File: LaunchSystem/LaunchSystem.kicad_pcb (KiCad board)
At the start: 2 copper layers, 125 x 50.5 mm, 24 parts, among them J1 GND - Ignition, J10 GND - Ignition, J2 VCC - +9V - Ignition, J5 VCC - 9V IN - ESP, J6 VCC - 9V IN - Ignition, J7 VCC - 9V IN - Ignition, J8 GND - Ignition, J9 GND - ESP, K1 43.41.7.005.2000, Q1 BC547, SW1 SW_SPDT, U2 L7805

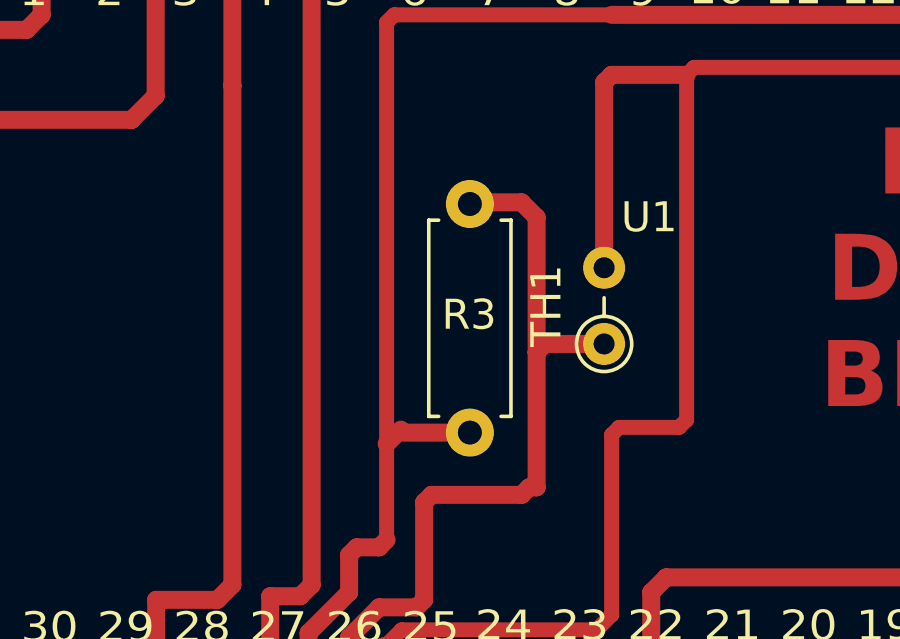
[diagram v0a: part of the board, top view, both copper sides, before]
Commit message: Update KiCad PWR section, footprints & nets
Add KiCad lock/history ignores to .gitignore. Major PCB changes: rename nets (GPIO35 -> 3.3v), add axial resistor footprint, replace/update TO-220 footprint for L7805 and update related pads/traces/zones. Schematic updates: bump sch revision to V3, add title block/date/rev/company, reposition components/junctions/wires, add PWR section label and a resistor symbol (R2), move PWR_FLAG and connectors. Overall: layout cleanup, footprint corrections and schematic revision to reflect PWR section rework.
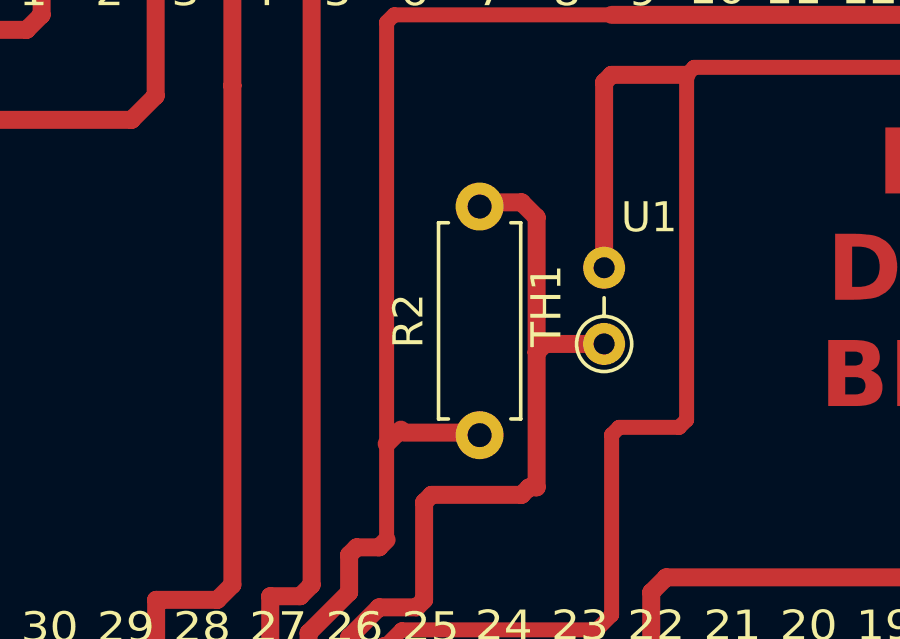
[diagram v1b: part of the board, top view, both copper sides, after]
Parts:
- removed R3: R 10k, Resistor_THT:R_Axial_DIN0207_L6.3mm_D2.5mm_P7.62mm_Horizontal
- added R2: R 10k, Resistor_THT:R_Axial_DIN0207_L6.3mm_D2.5mm_P7.62mm_Horizontal, F.Cu at (221.6, 98.0)
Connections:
- TH1 pad 1: Net-(U1-GPIO35) -> Net-(U1-3.3v)
- U1 pad 26: Net-(U1-GPIO35) -> Net-(U1-3.3v)
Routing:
- net Net-(U1-3.3v): track 294.4 -> 320.5 mm
- net Net-(U1-GPIO35): track 26.2 -> 0.00 mm

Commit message: Update LaunchSystem.kicad_pcb
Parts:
- J10, J8: value GND - Ignition -> GND - Ignition - Battery
- J6, J7: value VCC - 9V IN - Ignition -> VCC - 9V IN - Ignition Battery
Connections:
- R2 pad 2: Net-(U1-3.3v) -> Net-(U1-GPIO35)
- TH1 pad 1: Net-(U1-3.3v) -> Net-(U1-GPIO35)
- U1 pad 26: Net-(U1-3.3v) -> Net-(U1-GPIO35)
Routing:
- net Net-(U1-3.3v): track 320.5 -> 294.4 mm
- net Net-(U1-GPIO35): track 0.00 -> 26.2 mm
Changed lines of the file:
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@@
 			)
 		)
-		(property "Value" "VCC - 9V IN - Ignition"
+		(property "Value" "VCC - 9V IN - Ignition Battery"
 			(at 0 2.05 0)
 			(layer "F.Fab")
@@
 			(layers "*.Cu" "*.Mask")
 			(remove_unused_layers no)
-			(net "Net-(U1-3.3v)")
+			(net "Net-(U1-GPIO35)")
 			(pinfunction "GPIO35_26")
 			(pintype "bidirectional")
@@
 			(layers "*.Cu" "*.Mask")
 			(remove_unused_layers no)
-			(net "Net-(U1-3.3v)")
+			(net "Net-(U1-GPIO35)")
 			(pintype "passive")
 		)
@@
 			)
 		)
-		(property "Value" "VCC - 9V IN - Ignition"
+		(property "Value" "VCC - 9V IN - Ignition Battery"
 			(at 0 2.05 0)
 			(layer "F.Fab")
@@
 			(layers "*.Cu" "*.Mask")
 			(remove_unused_layers no)
-			(net "Net-(U1-3.3v)")
+			(net "Net-(U1-GPIO35)")
 			(pintype "passive")
 		)
@@
 			)
 		)
-		(property "Value" "GND - Ignition"
+		(property "Value" "GND - Ignition - Battery"
 			(at 0 2.05 0)
 			(layer "F.Fab")
@@
 			)
 		)
-		(property "Value" "GND - Ignition"
+		(property "Value" "GND - Ignition - Battery"
 			(at 6.975 6.975 0)
 			(layer "F.Fab")
@@
 	)
 	(segment
-		(start 223.78 94.97)
-		(end 223.5 95.25)
-		(width 0.6)
-		(layer "F.Cu")
-		(net "Net-(U1-3.3v)")
-	)
-	(segment
 		(start 210.818 108.318)
 		(end 210.818 103.5)
@@
 	)
 	(segment
-		(start 217.16 106.5)
-		(end 217.25 106.41)
-		(width 0.6)
-		(layer "F.Cu")
-		(net "Net-(U1-3.3v)")
-	)
-	(segment
-		(start 223.25 99.75)
-		(end 223.5 99.75)
-		(width 0.6)
-		(layer "F.Cu")
-		(net "Net-(U1-3.3v)")
-	)
-	(segment
-		(start 217.25 104.75)
-		(end 218.25 103.75)
-		(width 0.6)
-		(layer "F.Cu")
-		(net "Net-(U1-3.3v)")
-	)
-	(segment
 		(start 167.25 115.25)
 		(end 166.25 116.25)
@@
 	)
 	(segment
-		(start 221.33 90.25)
-		(end 223 90.25)
-		(width 0.6)
-		(layer "F.Cu")
-		(net "Net-(U1-3.3v)")
-	)
-	(segment
 		(start 217.25 103.25)
 		(end 217.25 102)
@@
 	)
 	(segment
-		(start 218.25 103.75)
-		(end 219.5 103.75)
-		(width 0.6)
-		(layer "F.Cu")
-		(net "Net-(U1-3.3v)")
-	)
-	(segment
 		(start 213.3586 86.3586)
 		(end 213.358 86.358)
@@
 	)
 	(segment
-		(start 217.25 106.41)
-		(end 217.25 104.75)
-		(width 0.6)
-		(layer "F.Cu")
-		(net "Net-(U1-3.3v)")
-	)
-	(segment
 		(start 141 117)
 		(end 140 118)
@@
 	)
 	(segment
-		(start 225.75 94.97)
-		(end 223.78 94.97)
-		(width 0.6)
-		(layer "F.Cu")
-		(net "Net-(U1-3.3v)")
-	)
-	(segment
-		(start 219.75 100.25)
-		(end 220 100)
-		(width 0.6)
-		(layer "F.Cu")
-		(net "Net-(U1-3.3v)")
-	)
-	(segment
 		(start 218.5 98.3)
 		(end 218.5 101.5)
@@
 	)
 	(segment
-		(start 219.75 103.5)
-		(end 219.75 100.25)
-		(width 0.6)
-		(layer "F.Cu")
-		(net "Net-(U1-3.3v)")
-	)
-	(segment
 		(start 218.5 84.25)
 		(end 218.75 84)
@@
 	)
 	(segment
-		(start 223.5 99.75)
-		(end 223.5 95.25)
-		(width 0.6)
-		(layer "F.Cu")
-		(net "Net-(U1-3.3v)")
-	)
-	(segment
 		(start 210.818 103.5)
 		(end 212.8586 103.5)
@@
 	)
 	(segment
-		(start 223 90.25)
-		(end 223.5 90.75)
-		(width 0.6)
-		(layer "F.Cu")
-		(net "Net-(U1-3.3v)")
-	)
-	(segment
-		(start 220 100)
-		(end 223 100)
-		(width 0.6)
-		(layer "F.Cu")
-		(net "Net-(U1-3.3v)")
-	)
-	(segment
 		(start 138.5 118.5)
 		(end 138.5 122.5)
@@
 	)
 	(segment
-		(start 223 100)
-		(end 223.25 99.75)
-		(width 0.6)
-		(layer "F.Cu")
-		(net "Net-(U1-3.3v)")
-	)
-	(segment
-		(start 219.5 103.75)
-		(end 219.75 103.5)
-		(width 0.6)
-		(layer "F.Cu")
-		(net "Net-(U1-3.3v)")
-	)
-	(segment
-		(start 223.5 90.75)
-		(end 223.5 95.25)
-		(width 0.6)
-		(layer "F.Cu")
-		(net "Net-(U1-3.3v)")
-	)
-	(segment
 		(start 131 77.5)
 		(end 130 78.5)
@@
 	)
 	(segment
-		(start 221.275 90.305)
-		(end 221.5 90.08)
-		(width 0.6)
-		(layer "F.Cu")
-		(net "Net-(U1-3.3v)")
-	)
-	(segment
-		(start 221.275 90.305)
-		(end 221.33 90.25)
-		(width 0.6)
-		(layer "F.Cu")
-		(net "Net-(U1-3.3v)")
-	)
-	(segment
 		(start 213.3586 103)
 		(end 213.3586 86.3586)
@@
 	)
 	(segment
+		(start 223.78 94.97)
+		(end 223.5 95.25)
+		(width 0.6)
+		(layer "F.Cu")
+		(net "Net-(U1-GPIO35)")
+	)
+	(segment
+		(start 217.16 106.5)
+		(end 217.25 106.41)
+		(width 0.6)
+		(layer "F.Cu")
+		(net "Net-(U1-GPIO35)")
+	)
+	(segment
+		(start 223.25 99.75)
+		(end 223.5 99.75)
+		(width 0.6)
+		(layer "F.Cu")
+		(net "Net-(U1-GPIO35)")
+	)
+	(segment
+		(start 217.25 104.75)
+		(end 218.25 103.75)
+		(width 0.6)
+		(layer "F.Cu")
+		(net "Net-(U1-GPIO35)")
+	)
+	(segment
+		(start 221.33 90.25)
+		(end 223 90.25)
+		(width 0.6)
+		(layer "F.Cu")
+		(net "Net-(U1-GPIO35)")
+	)
+	(segment
+		(start 218.25 103.75)
+		(end 219.5 103.75)
+		(width 0.6)
+		(layer "F.Cu")
+		(net "Net-(U1-GPIO35)")
+	)
+	(segment
+		(start 217.25 106.41)
+		(end 217.25 104.75)
+		(width 0.6)
+		(layer "F.Cu")
+		(net "Net-(U1-GPIO35)")
+	)
+	(segment
+		(start 225.75 94.97)
+		(end 223.78 94.97)
+		(width 0.6)
+		(layer "F.Cu")
+		(net "Net-(U1-GPIO35)")
+	)
+	(segment
+		(start 219.75 100.25)
+		(end 220 100)
+		(width 0.6)
+		(layer "F.Cu")
+		(net "Net-(U1-GPIO35)")
+	)
+	(segment
+		(start 219.75 103.5)
+		(end 219.75 100.25)
+		(width 0.6)
+		(layer "F.Cu")
+		(net "Net-(U1-GPIO35)")
+	)
+	(segment
+		(start 223.5 99.75)
+		(end 223.5 95.25)
+		(width 0.6)
+		(layer "F.Cu")
+		(net "Net-(U1-GPIO35)")
+	)
+	(segment
+		(start 223 90.25)
+		(end 223.5 90.75)
+		(width 0.6)
+		(layer "F.Cu")
+		(net "Net-(U1-GPIO35)")
+	)
+	(segment
+		(start 220 100)
+		(end 223 100)
+		(width 0.6)
+		(layer "F.Cu")
+		(net "Net-(U1-GPIO35)")
+	)
+	(segment
+		(start 223 100)
+		(end 223.25 99.75)
+		(width 0.6)
+		(layer "F.Cu")
+		(net "Net-(U1-GPIO35)")
+	)
+	(segment
+		(start 219.5 103.75)
+		(end 219.75 103.5)
+		(width 0.6)
+		(layer "F.Cu")
+		(net "Net-(U1-GPIO35)")
+	)
+	(segment
+		(start 223.5 90.75)
+		(end 223.5 95.25)
+		(width 0.6)
+		(layer "F.Cu")
+		(net "Net-(U1-GPIO35)")
+	)
+	(segment
+		(start 221.275 90.305)
+		(end 221.5 90.08)
+		(width 0.6)
+		(layer "F.Cu")
+		(net "Net-(U1-GPIO35)")
+	)
+	(segment
+		(start 221.275 90.305)
+		(end 221.33 90.25)
+		(width 0.6)
+		(layer "F.Cu")
+		(net "Net-(U1-GPIO35)")
+	)
+	(segment
